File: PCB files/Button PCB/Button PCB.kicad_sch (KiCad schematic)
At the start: 2 parts, among them SW1 TS-1102S-C-A-B, U1 X6511WVS-02H-C60D48R2

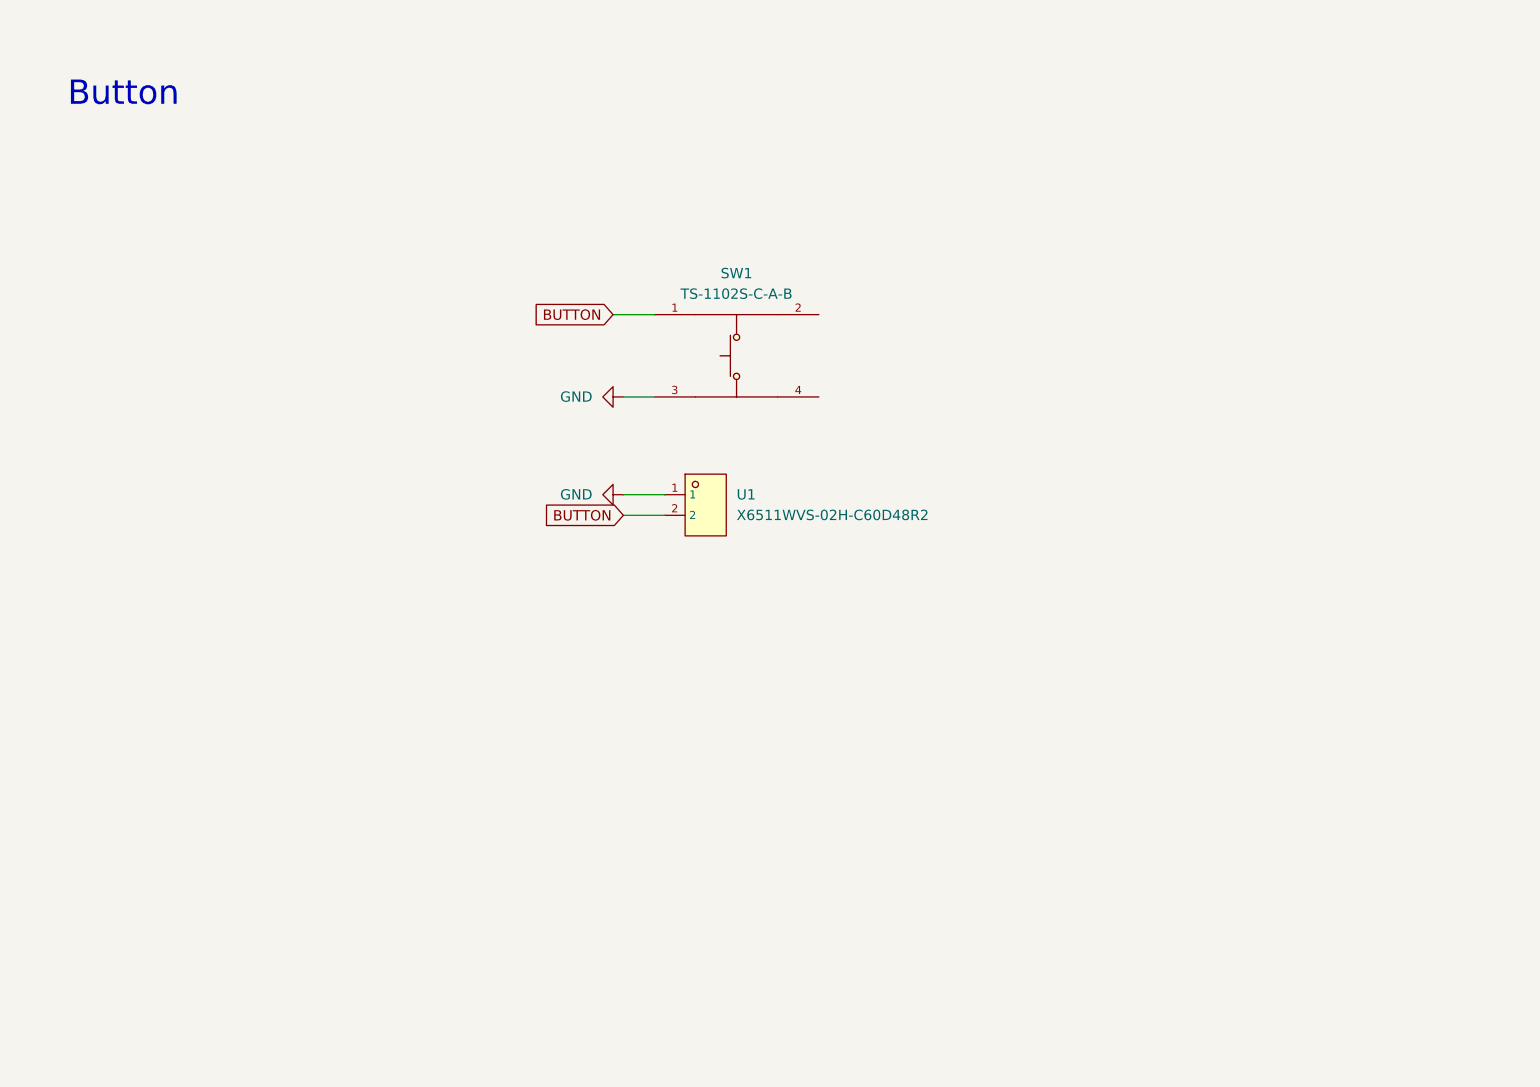
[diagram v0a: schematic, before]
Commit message: started redesign of pcb and added test for atopile
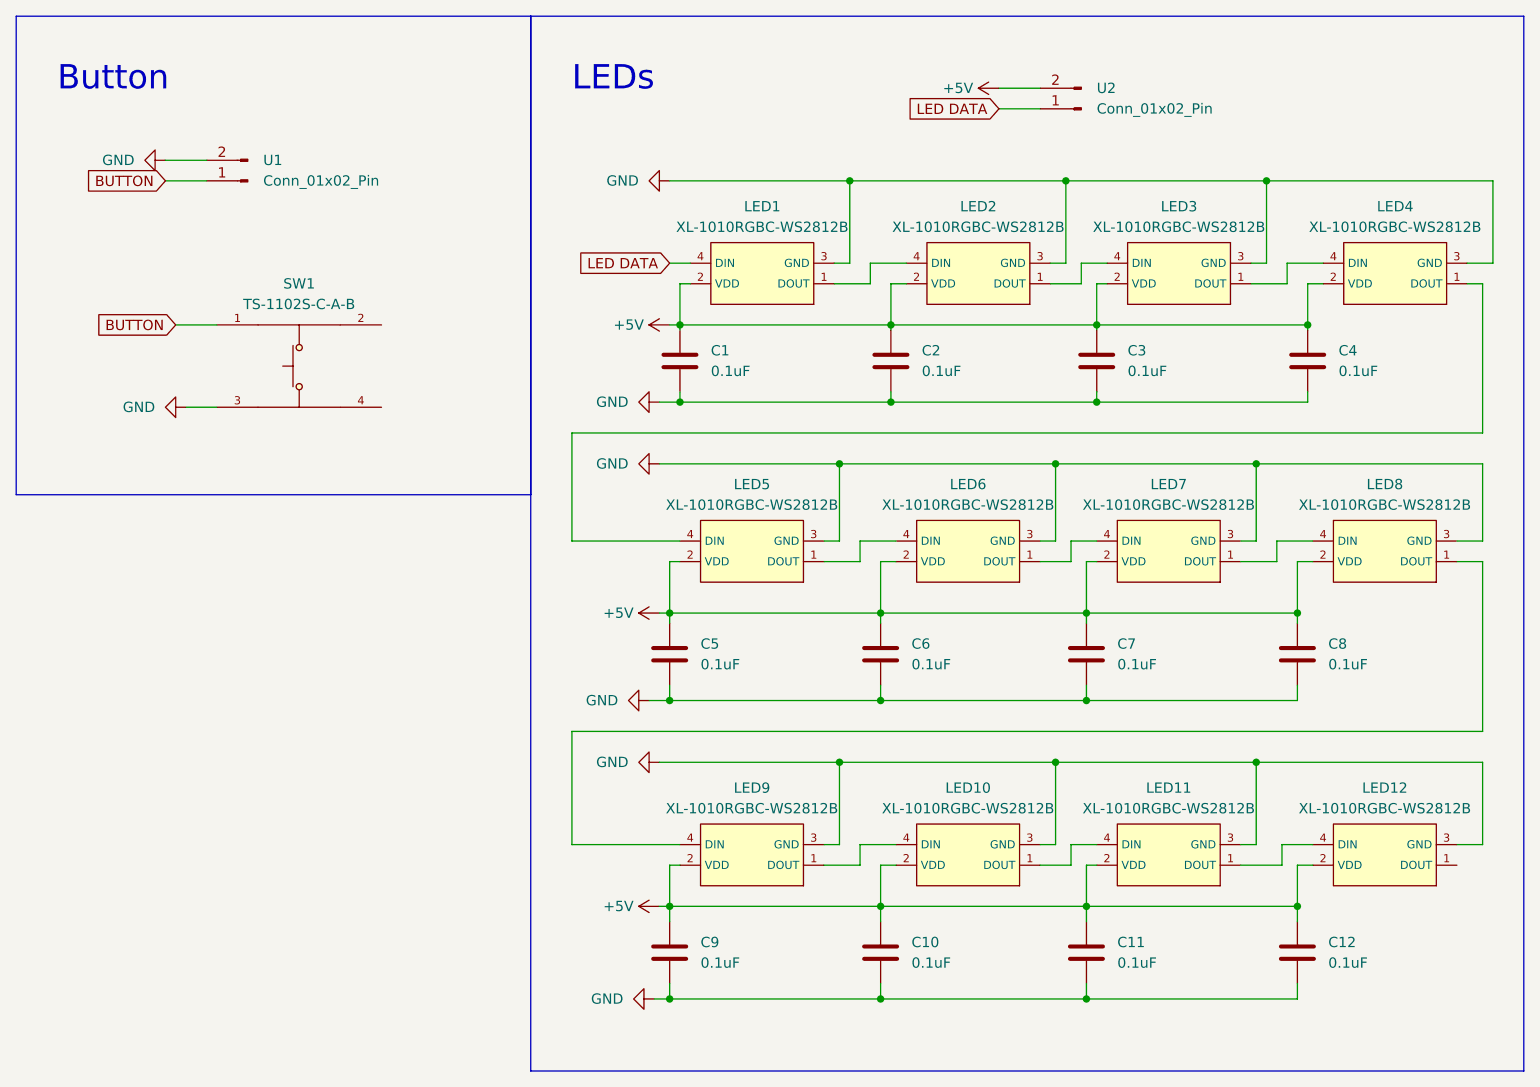
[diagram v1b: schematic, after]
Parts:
- removed U1: X6511WVS-02H-C60D48R2, footprint:HDR-SMD_2P-P2.54_XKB_X6511WVS-02H-C60D48R2, symbol MyParts:X6511WVS-02H-C60D48R2
- added C1, C10, C11, C12, C2, C3, C4, C5, C6, C7, C8, C9: 0.1uF, Capacitor_SMD:C_0402_1005Metric, symbol Device:C
- added LED1, LED10, LED11, LED12, LED2, LED3, LED4, LED5, LED6, LED7, LED8, LED9: XL-1010RGBC-WS2812B, footprint:LED-SMD_4P-L1.0-W1.0-TL_XL-1010RGBC-WS2812B, symbol MyParts:XL-1010RGBC-WS2812B
- added U1, U2: Conn_01x02_Pin, Connector_PinHeader_2.54mm:PinHeader_1x02_P2.54mm_Vertical, symbol Connector:Conn_01x02_Pin
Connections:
- net BUTTON: now also U1.1 (Pin_1)
- net GND: now also C1.2, C10.2, C11.2, C12.2, C2.2, C3.2, C4.2, C5.2, C6.2, C7.2, C8.2, C9.2, LED1.3 (GND), LED10.3 (GND), LED11.3 (GND), LED12.3 (GND), LED2.3 (GND), LED3.3 (GND), LED4.3 (GND), LED5.3 (GND), LED6.3 (GND), LED7.3 (GND), LED8.3 (GND), LED9.3 (GND), U1.2 (Pin_2)
- new net: LED3.1 (DOUT), LED4.4 (DIN)
- new net: LED2.1 (DOUT), LED3.4 (DIN)
- new net: LED8.1 (DOUT), LED9.4 (DIN)
- new net: LED7.1 (DOUT), LED8.4 (DIN)
- new net: LED10.1 (DOUT), LED11.4 (DIN)
- new net: LED10.4 (DIN), LED9.1 (DOUT)
- new net: LED6.1 (DOUT), LED7.4 (DIN)
- new net: LED5.1 (DOUT), LED6.4 (DIN)
- new net: LED1.1 (DOUT), LED2.4 (DIN)
- new net: LED4.1 (DOUT), LED5.4 (DIN)
- new net: LED11.1 (DOUT), LED12.4 (DIN)
- new net +5V: C1.1, C10.1, C11.1, C12.1, C2.1, C3.1, C4.1, C5.1, C6.1, C7.1, C8.1, C9.1, LED1.2 (VDD), LED10.2 (VDD), LED11.2 (VDD), LED12.2 (VDD), LED2.2 (VDD), LED3.2 (VDD), LED4.2 (VDD), LED5.2 (VDD), LED6.2 (VDD), LED7.2 (VDD), LED8.2 (VDD), LED9.2 (VDD), U2.2 (Pin_2)
- new net LED DATA: LED1.4 (DIN), U2.1 (Pin_1)
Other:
- note added: "LEDs"
- moved on the sheet: SW1
